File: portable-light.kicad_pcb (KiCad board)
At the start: 10 copper layers, 74 x 86.4 mm, 157 parts, among them J1 LOAD, J10 Charger, J2 conn_sense_pump_2, J3 conn_sense_buck_2, J4 conn_sense_pump_1, J5 conn_sense_buck_1, J6 interboard-interface_2, J7 interboard-interface_1, J8 Conn_01x05, J9 Conn_01x08, Q1 Q_PNP_BCE, Q10 S9012, Q11 S9012, Q12 MMBT2222, Q13 Q_NMOS_DGS, Q14 Q_PNP_BCE, Q15 Q_PNP_BCE, Q16 Q_PNP_BCE, Q17 Q_PNP_BCE, Q18 Q_PNP_BCE, Q19 Q_PNP_BCE, Q2 MMBT2222A, Q20 Q_PNP_BCE, Q21 MMBT2222, Q22 MMBT2222, Q23 MMBT2222, Q24 MMBT2222, Q25 Q_PNP_BCE, Q26 MMBT2222, Q27 Q_PNP_BCE, Q28 MMBT2222, Q29 PHD45N03LTA, Q3 MMBT2222, Q30 PHD45N03LTA, Q4 MMBT2222, Q5 MMBT2222, Q6 MMBT2222, Q7 S9012, Q8 MMBT2222, Q9 MMBT2222, U1 LTC1733EMSEPBF, U2 ATmega88PA-AU, U3 CD4094BPW, U4 L78L05_SOT89, Y1 20MHz Crystal

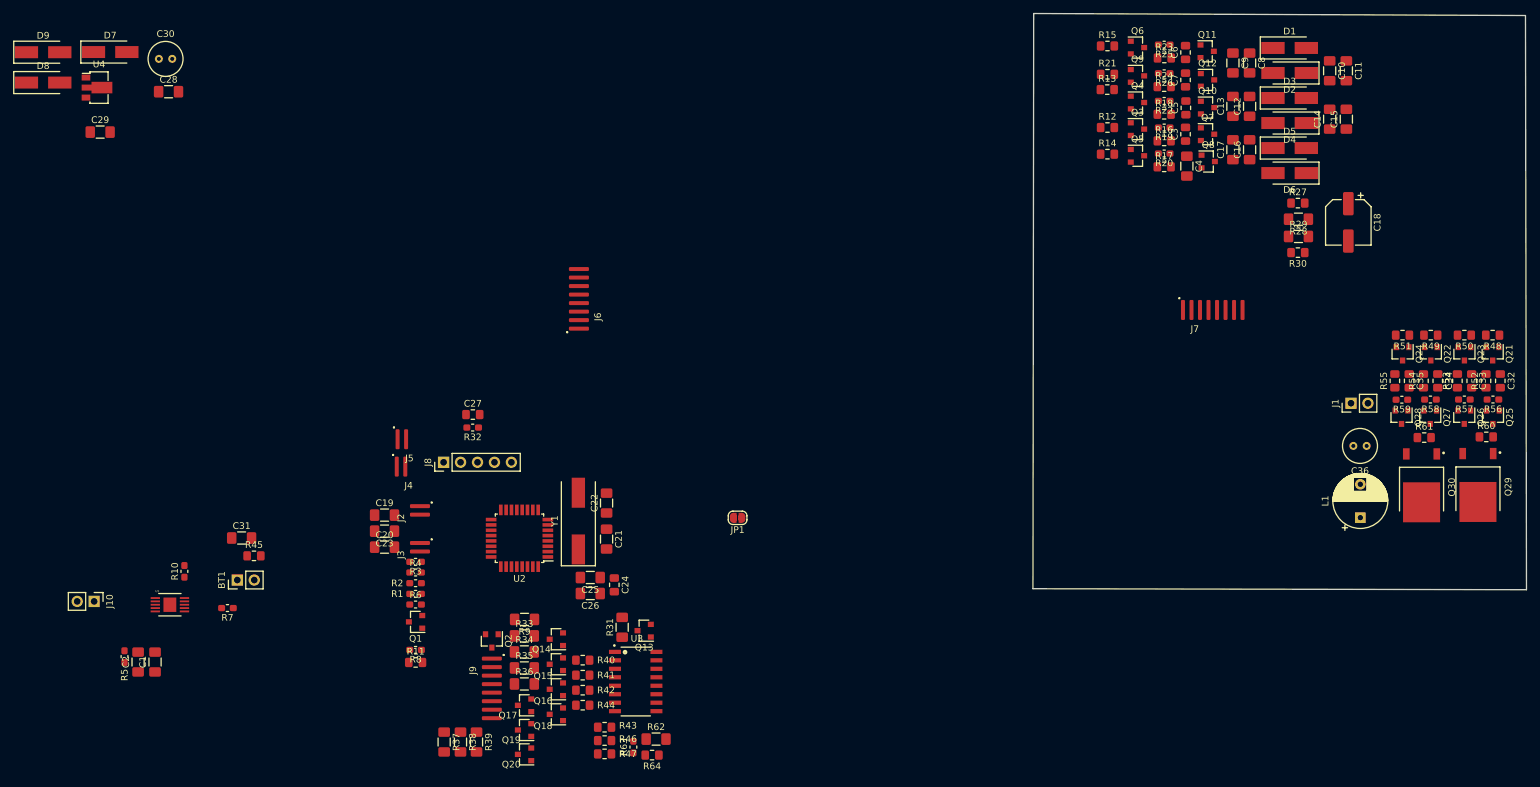
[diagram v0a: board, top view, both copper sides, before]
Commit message: Updated pcb from schem
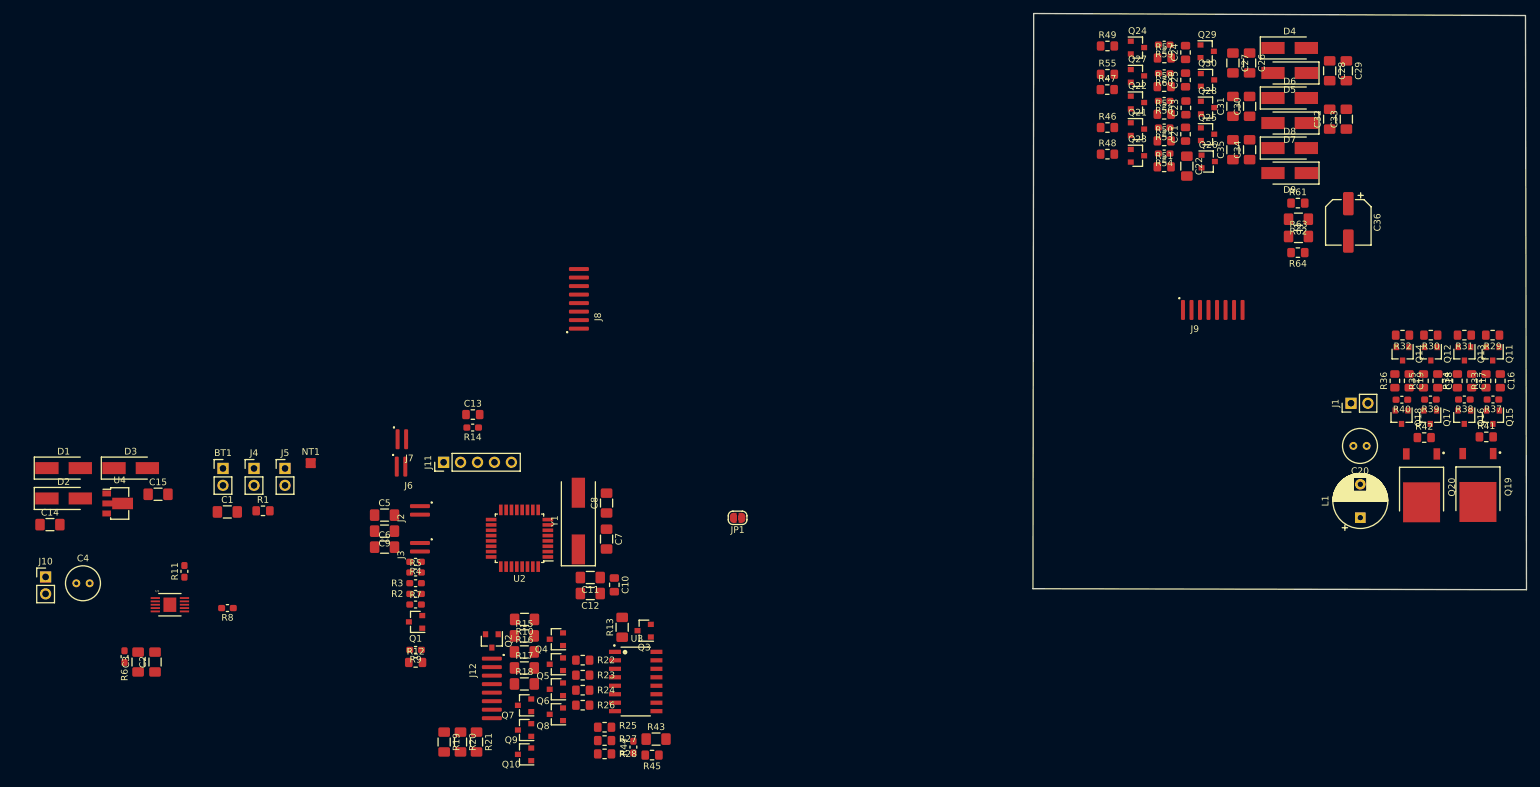
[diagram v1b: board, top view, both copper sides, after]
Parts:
- removed the C28 at (73.4, 30.6)
- removed the C29 at (63.1, 36.7)
- removed the C30 at (71.9, 25.7)
- removed the C31 at (84.3, 97.5)
- removed the D7 at (64.6, 24.7)
- removed the D8 at (54.6, 29.3)
- removed the D9 at (54.6, 24.7)
- removed the R45 at (86.2, 100.2)
- added C1: 330n, Capacitor_SMD:C_1206_3216Metric_Pad1.42x1.75mm_HandSolder, F.Cu at (82.2, 93.6)
- added C14: 100n, Capacitor_SMD:C_1206_3216Metric_Pad1.42x1.75mm_HandSolder, F.Cu at (55.6, 95.5)
- added C15: 100n, Capacitor_SMD:C_1206_3216Metric_Pad1.42x1.75mm_HandSolder, F.Cu at (71.8, 91.0)
- added C4: 10u, Capacitor_THT:C_Radial_D5.0mm_H7.0mm_P2.00mm, F.Cu at (59.5, 104.3)
- added D1: M7, Diode_SMD:D_SMA_Handsoldering, F.Cu at (57.6, 87.1)
- added D2: 1N5819, Diode_SMD:D_SMA_Handsoldering, F.Cu at (57.6, 91.6)
- added D3: 1N5819, Diode_SMD:D_SMA_Handsoldering, F.Cu at (67.7, 87.1)
- added J4: conn_batt_2, Connector_PinHeader_2.54mm:PinHeader_1x02_P2.54mm_Vertical, F.Cu at (86.2, 87.1)
- added J5: conn_batt_1, Connector_PinHeader_2.54mm:PinHeader_1x02_P2.54mm_Vertical, F.Cu at (90.8, 87.1)
- added NT1: Net-Tie_4_Cross, NetTie:NetTie-4_SMD_Pad0.5mm, F.Cu at (94.7, 86.3)
- added R1: 1R60, Resistor_SMD:R_0805_2012Metric_Pad1.15x1.40mm_HandSolder, F.Cu at (87.5, 93.5)
- moved U4 62.4 mm to (65.7, 92.4)
- moved BT1 16.9 mm to (81.5, 87.1), turned to 0 degrees
- moved J10 8.15 mm to (54.9, 103.4), turned to 0 degrees
- renumbered C24 to C10, C25 to C11, C26 to C12, C27 to C13, C32 to C16, C33 to C17, C34 to C18, C35 to C19, C1 to C2, C36 to C20, C3 to C21, C4 to C22, C5 to C23, C6 to C24, C7 to C25, C8 to C26, C9 to C27, C10 to C28, C11 to C29, C2 to C3, C12 to C30, C13 to C31, C14 to C32, C15 to C33, C16 to C34, C17 to C35, C18 to C36, C19 to C5, C20 to C6, C21 to C7, C22 to C8, C23 to C9, D1 to D4, D2 to D5, D3 to D6, D4 to D7, D5 to D8, D6 to D9, J8 to J11, J9 to J12, J4 to J6, J5 to J7, J6 to J8, J7 to J9, Q20 to Q10, Q21 to Q11, Q22 to Q12, Q23 to Q13, Q24 to Q14, Q25 to Q15, Q26 to Q16, Q27 to Q17, Q28 to Q18, Q29 to Q19, Q30 to Q20, Q3 to Q21, Q4 to Q22, Q5 to Q23, Q6 to Q24, Q7 to Q25, Q8 to Q26, Q9 to Q27, Q10 to Q28, Q11 to Q29, Q13 to Q3, Q12 to Q30, Q14 to Q4, Q15 to Q5, Q16 to Q6, Q17 to Q7, Q18 to Q8, Q19 to Q9, R9 to R10, R10 to R11, R11 to R12, R31 to R13, R32 to R14, R33 to R15, R34 to R16, R35 to R17, R36 to R18, R37 to R19, R1 to R2, R38 to R20, R39 to R21, R40 to R22, R41 to R23, R42 to R24, R43 to R25, R44 to R26, R46 to R27, R47 to R28, R48 to R29, R2 to R3, R49 to R30, R50 to R31, R51 to R32, R52 to R33, R53 to R34, R54 to R35, R55 to R36, R56 to R37, R57 to R38, R58 to R39, R3 to R4, R59 to R40, R60 to R41, R61 to R42, R62 to R43, R63 to R44, R64 to R45, R12 to R46, R13 to R47, R14 to R48, R15 to R49, R4 to R5, R16 to R50, R17 to R51, R18 to R52, R19 to R53, R20 to R54, R21 to R55, R22 to R56, R23 to R57, R24 to R58, R25 to R59, R5 to R6, R26 to R60, R27 to R61, R28 to R62, R29 to R63, R30 to R64, R6 to R7, R7 to R8, R8 to R9
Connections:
- net VDC renamed +CHARGER
- BT1 pad 1: +BATT -> +BATT-2
- BT1 pad 2: GNDPWR -> GND
- C10 pad 2: VBUS -> +5V
- C11 pad 2: VBUS -> +5V
- C12 pad 2: VBUS -> +5V
- C2 pad 2: GNDPWR -> GND-CHARGER
- C3 pad 2: GNDPWR -> GND-CHARGER
- C36 pad 1: +8V -> +PUMP-1
- D9 pad 1: +8V -> +PUMP-1
- J10 pad 2: GNDPWR -> GND-CHARGER
- J6 pad 1: GNDA -> /gnd_vsense_pump_1
- J6 pad 2: (no net) -> /vsense_pump_1
- J7 pad 1: GNDA -> /gnd_vsense_buck_1
- J7 pad 2: (no net) -> /vsense_buck_1
- J8 pad 5: +8V -> +PUMP-2
- J9 pad 5: +8V -> +PUMP-1
- Q1 pad 2: +BATT -> +BATT-2
- Q10 pad 2: VBUS -> +5V
- Q15 pad 2: VBUS -> +PUMP-1
- Q17 pad 2: VBUS -> +PUMP-1
- Q19 pad 4: +BATT -> +BATT-1
- Q2 pad 2: GND -> GND-CHARGER
- Q25 pad 2: +BATT -> +BATT-1
- Q28 pad 2: +BATT -> +BATT-1
- Q29 pad 2: +BATT -> +BATT-1
- Q4 pad 2: VBUS -> +5V
- Q5 pad 2: VBUS -> +5V
- Q6 pad 2: VBUS -> +5V
- Q7 pad 2: VBUS -> +5V
- Q8 pad 2: VBUS -> +5V
- Q9 pad 2: VBUS -> +5V
- R4 pad 1: VBUS -> +5V
- R44 pad 1: /vsense_buck -> /vsense_buck_1
- R45 pad 1: GND -> /gnd_vsense_buck_1
- R45 pad 2: /vsense_buck -> /vsense_buck_1
- R61 pad 1: +8V -> +PUMP-1
- R61 pad 2: /vsense_pump -> /vsense_pump_1
- R62 pad 1: /vsense_pump -> /vsense_pump_1
- R64 pad 2: GND -> /gnd_vsense_pump_1
- U1 pad 11: GNDPWR -> GND-CHARGER
- U1 pad 5: GNDPWR -> GND-CHARGER
- U1 pad 6: GNDPWR -> GND-CHARGER
- U1 pad 9: +BATT -> +BATT-2
- U2 pad 18: VBUS -> +5V
- U2 pad 4: VBUS -> +5V
- U2 pad 6: VBUS -> +5V
- U3 pad 10: (no net) -> Net-(U3-Pad10)
- U3 pad 11: (no net) -> Net-(U3-Pad11)
- U3 pad 16: VBUS -> +5V
- U3 pad 9: (no net) -> Net-(U3-Pad9)
- U4 pad 2: GNDPWR -> GND
- U4 pad 3: +8V -> +PUMP-2

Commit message: Cleaned up the PCB a little bit, Fixed some errors in schematics
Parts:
- moved J7 127.7 mm to (228.4, 124.5), turned to 180 degrees
- moved J6 122.1 mm to (229.4, 94.4)
- moved J5 120.2 mm to (210.9, 83.5), turned to 90 degrees
- moved R44 82.5 mm to (225.0, 120.0)
- moved R45 82.5 mm to (227.8, 121.2)
- moved R43 82.5 mm to (228.4, 118.8)
- moved R10 60.1 mm to (74.1, 138.7), turned to 0 degrees
- moved C14 56.9 mm to (111.7, 104.8)
- moved D1 55.0 mm to (111.7, 97.2)
- moved D3 55.0 mm to (121.7, 97.5)
- moved U4 55.0 mm to (119.7, 102.8)
- moved D2 55.0 mm to (111.7, 101.4)
- moved C15 53.9 mm to (124.3, 102.8), turned to 270 degrees
- moved R19 52.0 mm to (78.6, 165.5)
- moved Q4 52.0 mm to (95.4, 150.1)
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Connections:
- D3 pad 2: +BATT-1 -> +BATT-2
- J8 pad 1: /buck_low_mos_low_bjt_2 -> /buck_low_mos_high_bjt_2
- J8 pad 2: /buck_low_mos_high_bjt_2 -> /buck_low_mos_low_bjt_2
- J8 pad 7: /pump_clkb_2 -> /pump_clka_2
- J8 pad 8: /pump_clka_2 -> /pump_clkb_2
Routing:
- net +CHARGER: track 0.00 -> 15.7 mm
- net Net-(R8-Pad2): track 0.00 -> 14.4 mm
- net Net-(Q1-Pad3): track 0.00 -> 14.3 mm
- net /vsense_pump_2: track 0.00 -> 13.7 mm
- net /vsense_buck_2: track 0.00 -> 13.3 mm
- net Net-(C9-Pad1): track 0.00 -> 12.0 mm
- net +BATT-2: track 0.00 -> 11.9 mm
- net Net-(C2-Pad1): track 0.00 -> 11.4 mm
- net Net-(R6-Pad2): track 0.00 -> 10.7 mm
- net GND-CHARGER: track 0.00 -> 8.28 mm
- net GND: track 0.00 -> 4.21 mm
- net GNDPWR-2: track 0.00 -> 3.44 mm
- net Net-(R11-Pad1): track 0.00 -> 3.13 mm
- net Net-(Q2-Pad3): track 0.00 -> 2.96 mm
- net Net-(R12-Pad1): track 0.00 -> 2.59 mm
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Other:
- board size 74 x 86.4 mm -> 74 x 86.3 mm

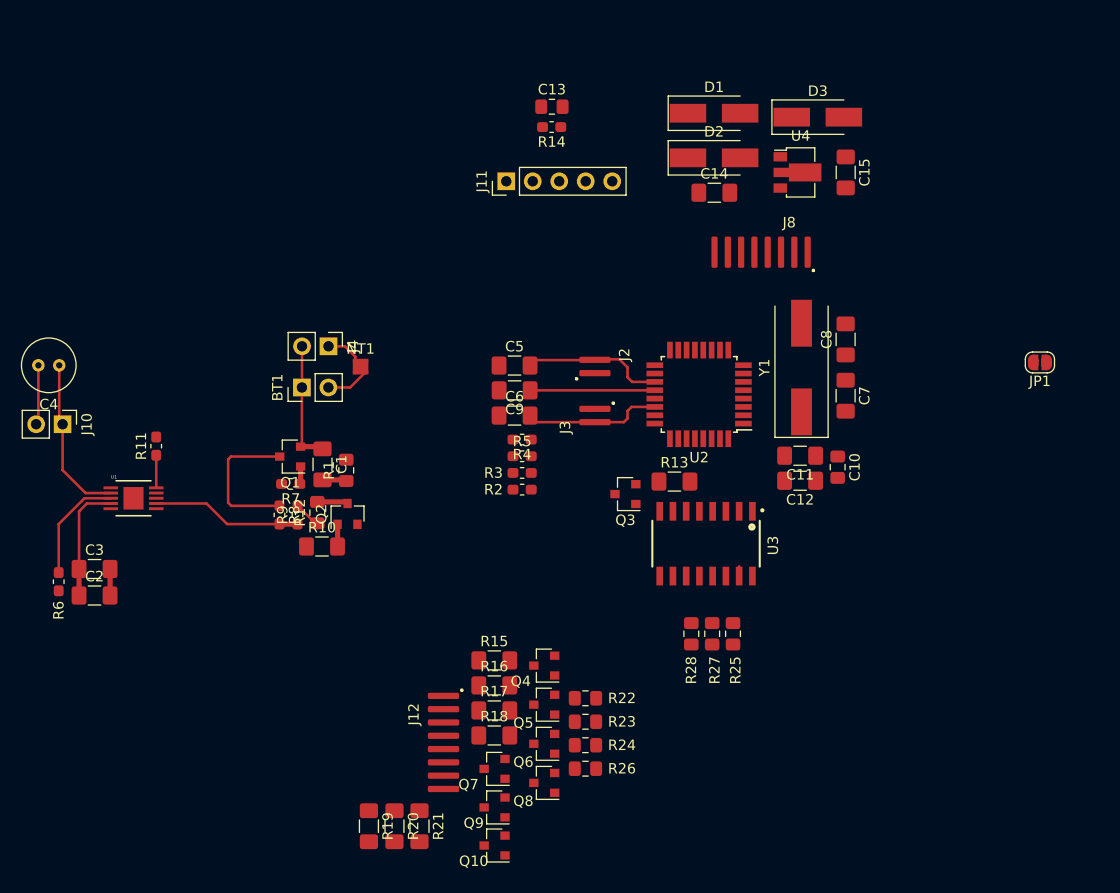
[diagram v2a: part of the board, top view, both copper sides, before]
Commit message: Fixed some minor stuff in schematics, Refined the PCB a little bit more
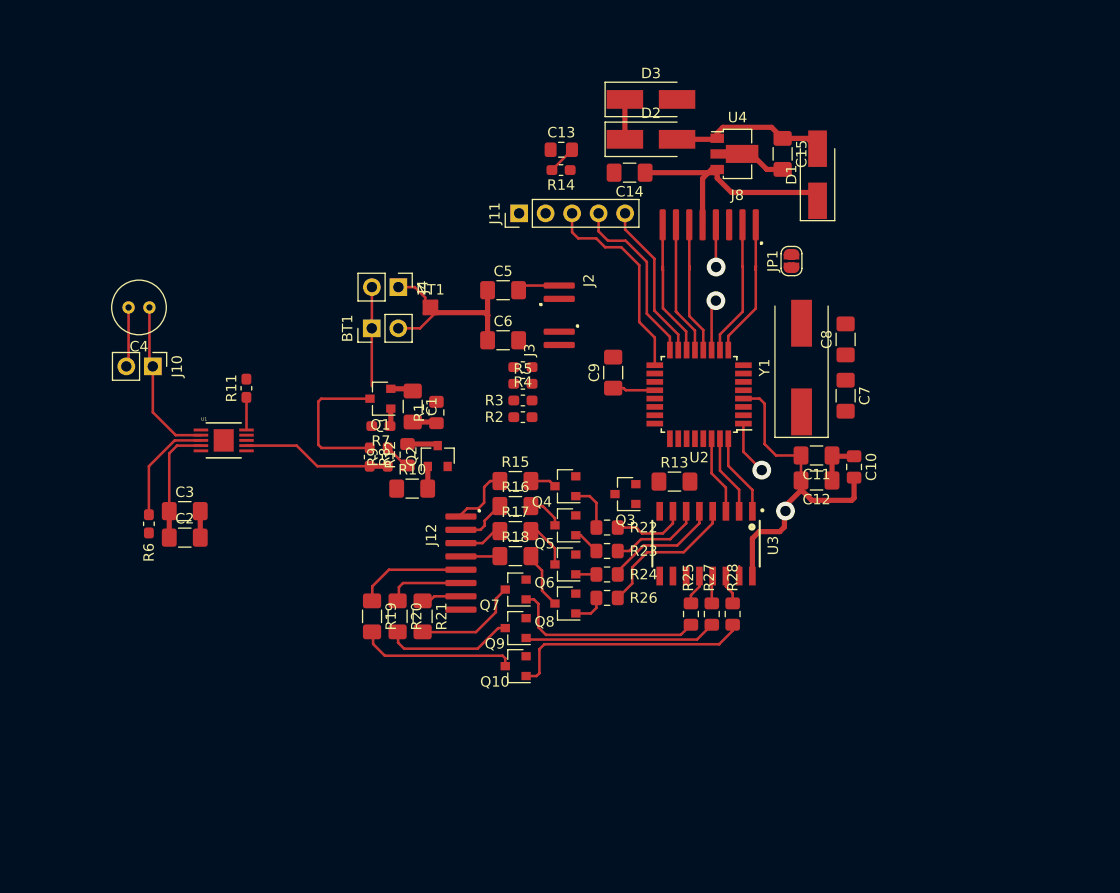
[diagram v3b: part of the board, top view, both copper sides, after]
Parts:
- moved JP1 25.7 mm to (119.1, 111.3), turned to 90 degrees
- moved R19 20.1 mm to (78.9, 145.4)
- moved R20 20.1 mm to (81.3, 145.4)
- moved R21 20.1 mm to (83.8, 145.4)
- moved Q7 17.3 mm to (92.7, 142.8)
- moved R15 17.3 mm to (92.6, 132.4)
- moved Q4 17.3 mm to (97.4, 132.9)
- moved Q5 17.3 mm to (97.4, 136.7)
- moved Q6 17.3 mm to (97.4, 140.4)
- moved Q8 17.3 mm to (97.4, 144.2)
- moved R16 17.3 mm to (92.6, 134.8)
- moved R17 17.3 mm to (92.6, 137.2)
- moved R18 17.3 mm to (92.6, 139.6)
- moved Q10 17.3 mm to (92.7, 150.2)
- moved Q9 17.3 mm to (92.7, 146.5)
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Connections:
- R22 pad 2: /Controller/seg-base-1 -> /Controller/seg-base-4
- R23 pad 2: /Controller/seg-base-2 -> /Controller/seg-base-3
- R24 pad 2: /Controller/seg-base-3 -> /Controller/seg-base-2
- R25 pad 2: /Controller/seg-base-5 -> /Controller/seg-base-7
- R26 pad 2: /Controller/seg-base-4 -> /Controller/seg-base-1
- R28 pad 2: /Controller/seg-base-7 -> /Controller/seg-base-5
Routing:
- net +5V: track 0.00 -> 37.0 mm, vias 0 -> 1
- net +PUMP-2: track 0.00 -> 24.6 mm
- net Net-(Q10-Pad1): track 0.00 -> 23.5 mm
- net GND: track 4.21 -> 25.5 mm
- net /Controller/sck: track 0.00 -> 19.8 mm
- net Net-(Q7-Pad1): track 0.00 -> 18.9 mm
- net Net-(Q9-Pad1): track 0.00 -> 18.5 mm
- net /Controller/miso: track 0.00 -> 16.9 mm
- net /Controller/seg-5: track 0.00 -> 15.3 mm
- net /Controller/mosi: track 0.00 -> 15.2 mm
- net Net-(C15-Pad1): track 0.00 -> 15.1 mm
- net /Controller/seg-base-1: track 0.00 -> 14.1 mm
- net /pump_clka_2: track 0.00 -> 13.7 mm
- net /buck_low_mos_high_bjt_2: track 0.00 -> 13.5 mm
- net /pump_clkb_2: track 0.00 -> 13.4 mm
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
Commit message: Seperated the two PCBs successfully, All DRC errors fixed, gotta double check the circuit
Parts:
- removed JP1: Jumper_Mosfet_Open, Jumper:SolderJumper-2_P1.3mm_Open_RoundedPad1.0x1.5mm
- added J13: Conn_01x02-Connector_Generic, Ribbon_Cable:Ribbon_2, F.Cu at (95.6, 82.8)
- NT1: value Net-Tie_4_Cross -> Net-Tie_3_Tee; footprint NetTie:NetTie-4_SMD_Pad0.5mm -> NetTie:NetTie-3_SMD_Pad0.5mm
- moved Q20 65.9 mm to (180.8, 138.5)
- moved C16 65.1 mm to (193.5, 123.0)
- moved C17 65.1 mm to (189.2, 123.0)
- moved Q18 65.1 mm to (178.7, 128.4)
- moved R36 65.1 mm to (177.7, 123.0)
- moved C18 65.1 mm to (184.2, 123.0)
- moved C19 65.1 mm to (179.9, 123.0)
- moved Q11 65.1 mm to (192.4, 118.9)
- moved Q12 65.1 mm to (183.1, 118.9)
- moved Q13 65.1 mm to (188.2, 118.9)
- moved Q14 65.1 mm to (178.9, 118.9)
- moved Q15 65.1 mm to (192.4, 128.4)
- moved Q16 65.1 mm to (188.1, 128.4)
- moved Q17 65.1 mm to (183.0, 128.4)
- moved R29 65.1 mm to (192.4, 116.1)
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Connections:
- BT1 pad 2: GND -> GND-CHARGER
- C12 pad 1: GND -> GNDA
- C5 pad 1: GND -> GNDA
- C6 pad 1: GND -> GNDA
- C9 pad 2: GND -> GNDA
- J11 pad 5: /Controller/mosi -> /buck_high_mos_low_bjt_2
- J4 pad 1: GNDPWR-2 -> GND-CHARGER
- NT1 pad 1: GNDPWR-2 -> GND-CHARGER
- NT1 pad 2: GND-CHARGER -> GNDA
- NT1 pad 3: GNDA -> GND
- R1 pad 2: GND -> GND-CHARGER
- U2 pad 15: /Controller/mosi -> /buck_high_mos_low_bjt_2
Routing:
- net +5V: track 37.0 -> 204.1 mm, vias 1 -> 3
- net +PUMP-1: track 0.00 -> 128.1 mm, vias 0 -> 3
- net +BATT-1: track 0.00 -> 84.8 mm, vias 0 -> 1
- net +BATT-2: track 11.9 -> 88.5 mm, vias 0 -> 1
- net /Controller/charger_fault_in: track 0.00 -> 47.6 mm, vias 0 -> 2
- net /Controller/charger_chrg_in: track 0.00 -> 47.4 mm, vias 0 -> 2
- net /Controller/reset: track 0.00 -> 44.9 mm, vias 0 -> 1
- net Net-(C28-Pad2): track 0.00 -> 44.5 mm
- net /buck_high_mos_low_bjt_2: track 0.00 -> 43.0 mm, vias 0 -> 1
- net /Controller/shiftregister-vss: track 5.07 -> 43.3 mm, vias 1 -> 2
- net GND-CHARGER: track 8.28 -> 41.6 mm, vias 0 -> 4
- net /pump_clkb_1: track 0.00 -> 28.3 mm
- net Net-(L1-Pad1): track 0.00 -> 27.7 mm
- net Net-(C26-Pad2): track 0.00 -> 26.0 mm
- net Net-(D4-Pad2): track 0.00 -> 25.1 mm
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- added copper zone on F.Cu, net GND
- added copper zone on F.Cu, net GND-CHARGER
- added copper zone on F.Cu, net GNDA
- added copper zone on F.Cu, net GNDPWR
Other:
- board size 74 x 86.3 mm -> 171.2 x 130.2 mm
